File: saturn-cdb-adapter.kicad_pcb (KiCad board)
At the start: 2 copper layers, 76.2 x 76.2 mm, 60 parts, among them P1 CONN_02X22, P2 CONN_02X20, P3 CONN_02X20, P4 CONN_02X20, P5 CONN_02X20, U1 SH1, U2 MT28EW_FLASH

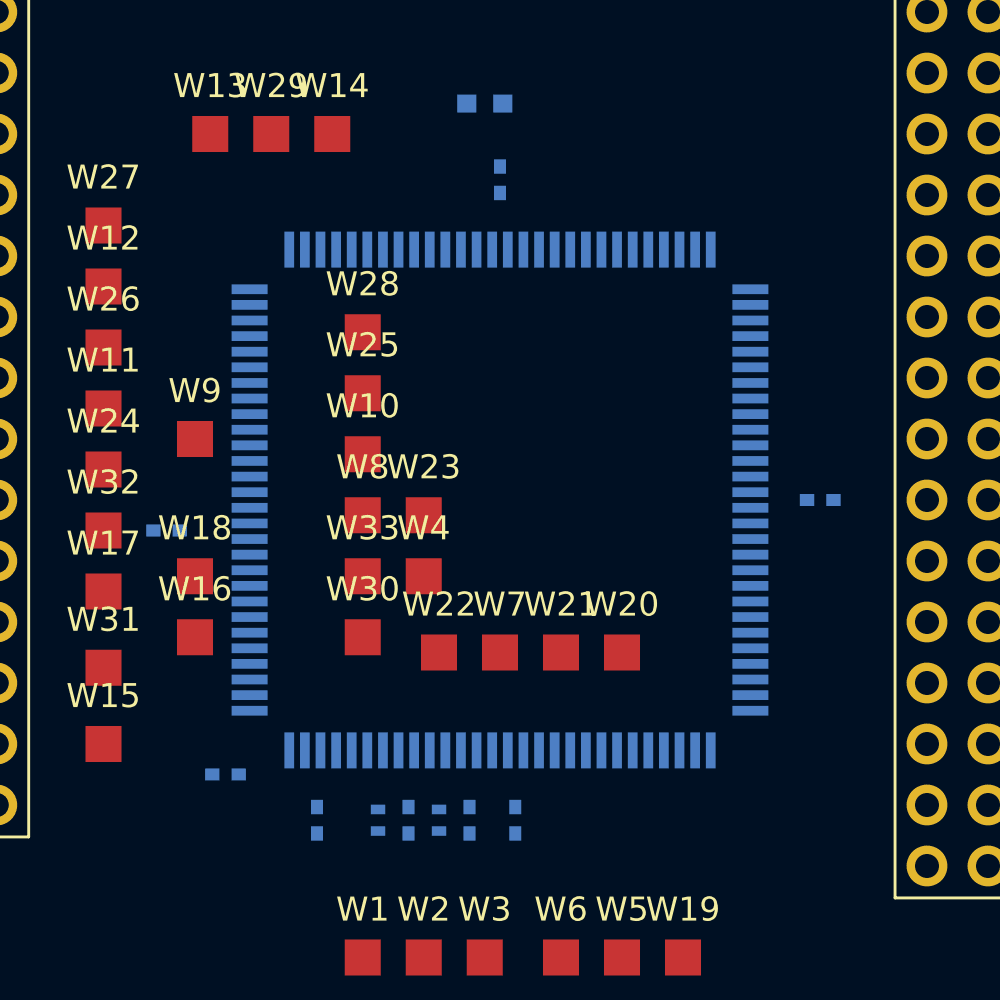
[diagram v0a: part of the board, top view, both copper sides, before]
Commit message: Fix sh1 footprint some more
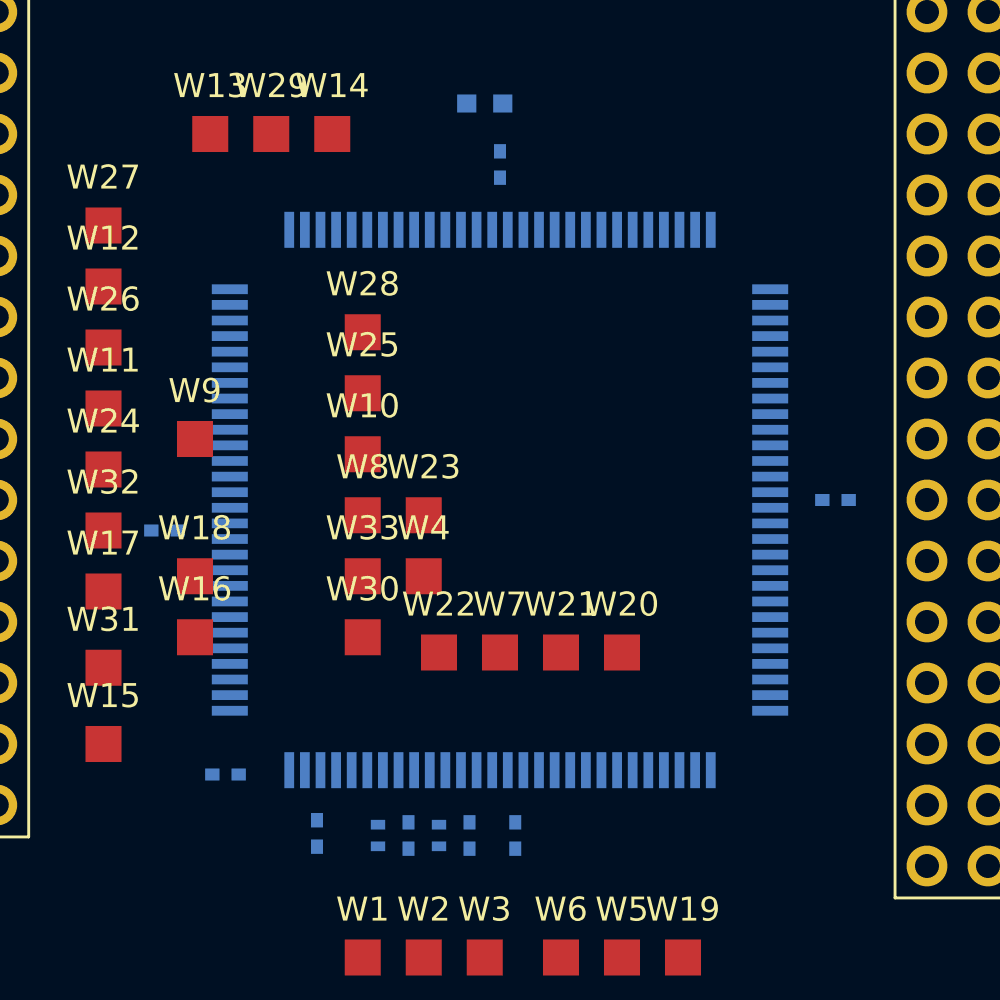
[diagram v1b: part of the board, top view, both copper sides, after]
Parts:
- moved C2 0.64 mm to (100.3, 99.1)
- moved C3 0.64 mm to (87.0, 113.0)
- moved C4 0.64 mm to (85.1, 113.0)
- moved C5 0.64 mm to (82.5, 113.0)
- moved R1 0.64 mm to (81.3, 113.0)
- moved R2 0.64 mm to (83.8, 113.0)
- moved C1 0.63 mm to (86.4, 85.1)
- moved C6 0.55 mm to (78.7, 112.9)
- moved C8 0.08 mm to (72.4, 100.3)

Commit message: More minor adjustments
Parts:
- moved W23 13.4 mm to (69.8, 99.1)
- moved W30 11.0 mm to (69.8, 106.7)
- moved W10 10.8 mm to (69.8, 96.5)
- moved W33 10.8 mm to (69.8, 101.6)
- moved W15 9.16 mm to (77.5, 104.1)
- moved W8 8.25 mm to (72.4, 99.7)
- moved W27 8.03 mm to (77.5, 90.2)
- moved W32 7.73 mm to (77.5, 101.6)
- moved C12 6.02 mm to (91.4, 84.5)
- moved W28 5.46 mm to (77.5, 87.6)
- moved W18 4.96 mm to (77.5, 99.1)
- moved W4 4.84 mm to (81.3, 106.7)
- moved W13 4.26 mm to (72.4, 87.6)
- moved W16 3.86 mm to (69.8, 104.1)
- moved W9 3.81 mm to (77.5, 96.5)
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
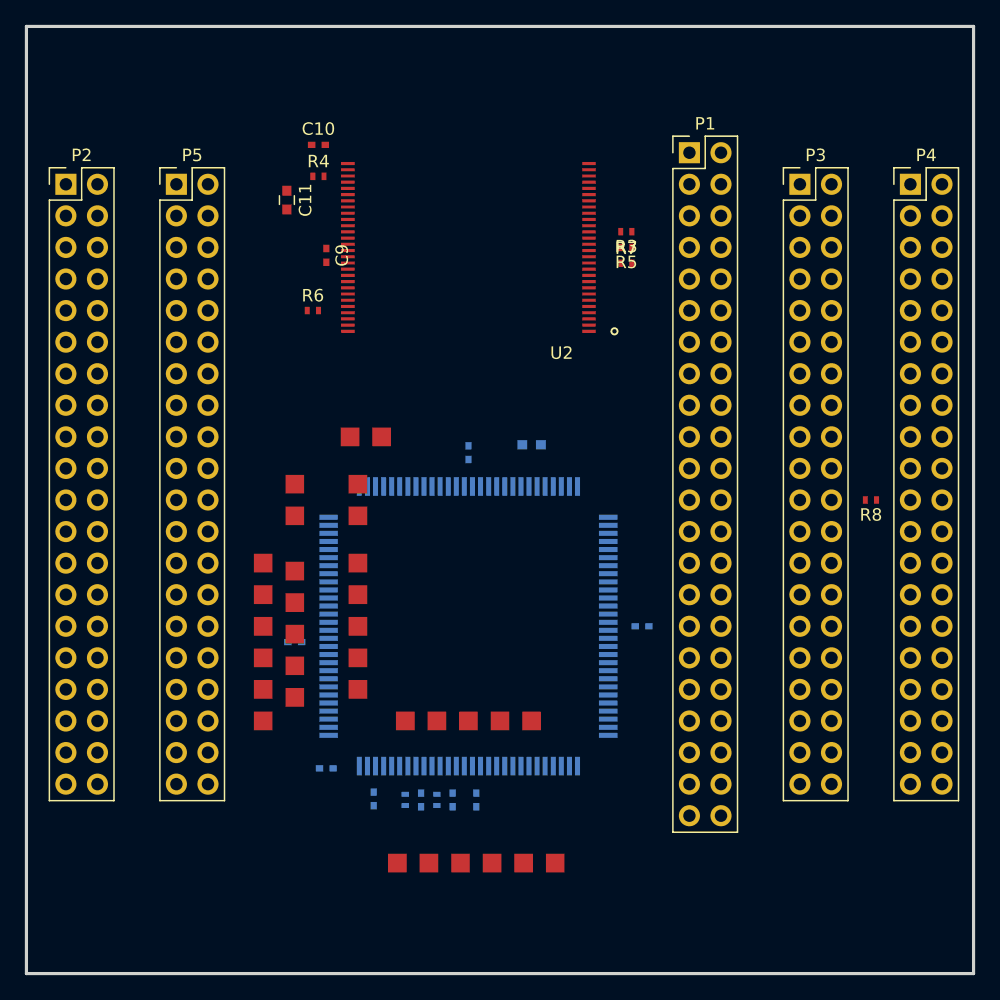
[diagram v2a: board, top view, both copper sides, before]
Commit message: Initial very rough route for most signals
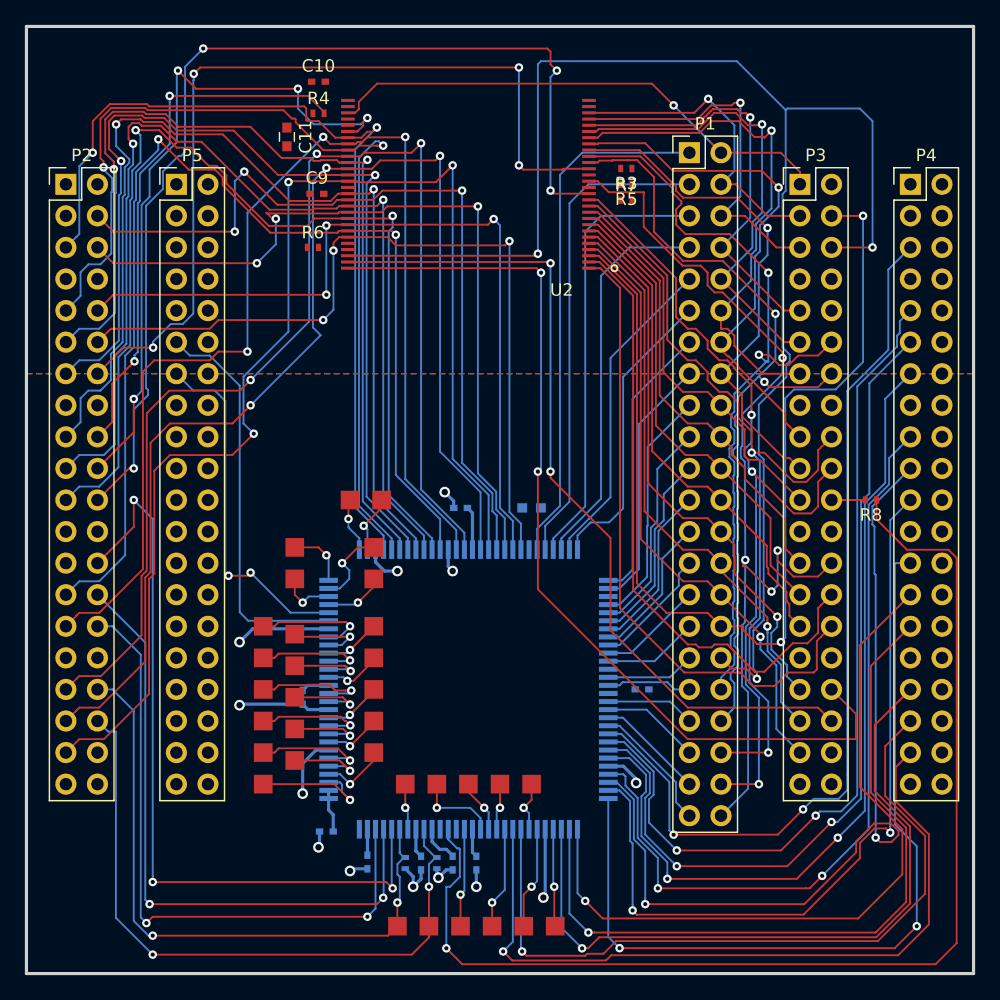
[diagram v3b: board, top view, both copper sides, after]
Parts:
- moved W32 5.24 mm to (78.7, 106.7)
- moved W15 5.24 mm to (78.7, 109.2)
- moved W18 5.24 mm to (78.7, 104.1)
- moved W25 5.24 mm to (78.7, 99.1)
- moved W27 5.24 mm to (78.7, 95.2)
- moved W28 5.24 mm to (78.7, 92.7)
- moved W9 5.24 mm to (78.7, 101.6)
- moved C6 5.11 mm to (78.2, 118.0)
- moved W14 5.08 mm to (79.4, 88.9)
- moved W29 5.08 mm to (76.8, 88.9)
- moved W33 5.08 mm to (69.8, 106.7)
- moved W8 5.08 mm to (72.4, 104.8)
- moved C10 5.08 mm to (74.3, 55.2)
- moved R3 5.08 mm to (99.1, 62.2)
- moved R4 5.08 mm to (74.3, 57.8)
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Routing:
- net FLASH_A16: track 0.00 -> 124.5 mm, vias 0 -> 3
- net AD11: track 0.00 -> 104.0 mm, vias 0 -> 3
- net AD10: track 0.00 -> 100.2 mm, vias 0 -> 3
- net AD9: track 0.00 -> 98.9 mm, vias 0 -> 3
- net AD8: track 0.00 -> 94.8 mm, vias 0 -> 3
- net CPU_CLK: track 0.00 -> 93.2 mm, vias 0 -> 1
- net AD7: track 0.00 -> 90.2 mm, vias 0 -> 2
- net AD6: track 0.00 -> 86.3 mm, vias 0 -> 2
- net AD5: track 0.00 -> 84.4 mm, vias 0 -> 2
- net FLASH_A15: track 0.00 -> 83.8 mm, vias 0 -> 2
- net ~FLASH_WE: track 0.00 -> 83.2 mm, vias 0 -> 4
- net AD4: track 0.00 -> 82.7 mm, vias 0 -> 2
- net AD3: track 0.00 -> 78.9 mm, vias 0 -> 2
- net AD1: track 0.00 -> 78.0 mm, vias 0 -> 2
- net FLASH_A21: track 0.00 -> 76.9 mm, vias 0 -> 4
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- added copper zone on B.Cu, net GND
- added copper zone on F.Cu, net GND

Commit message: Initial all signals connected
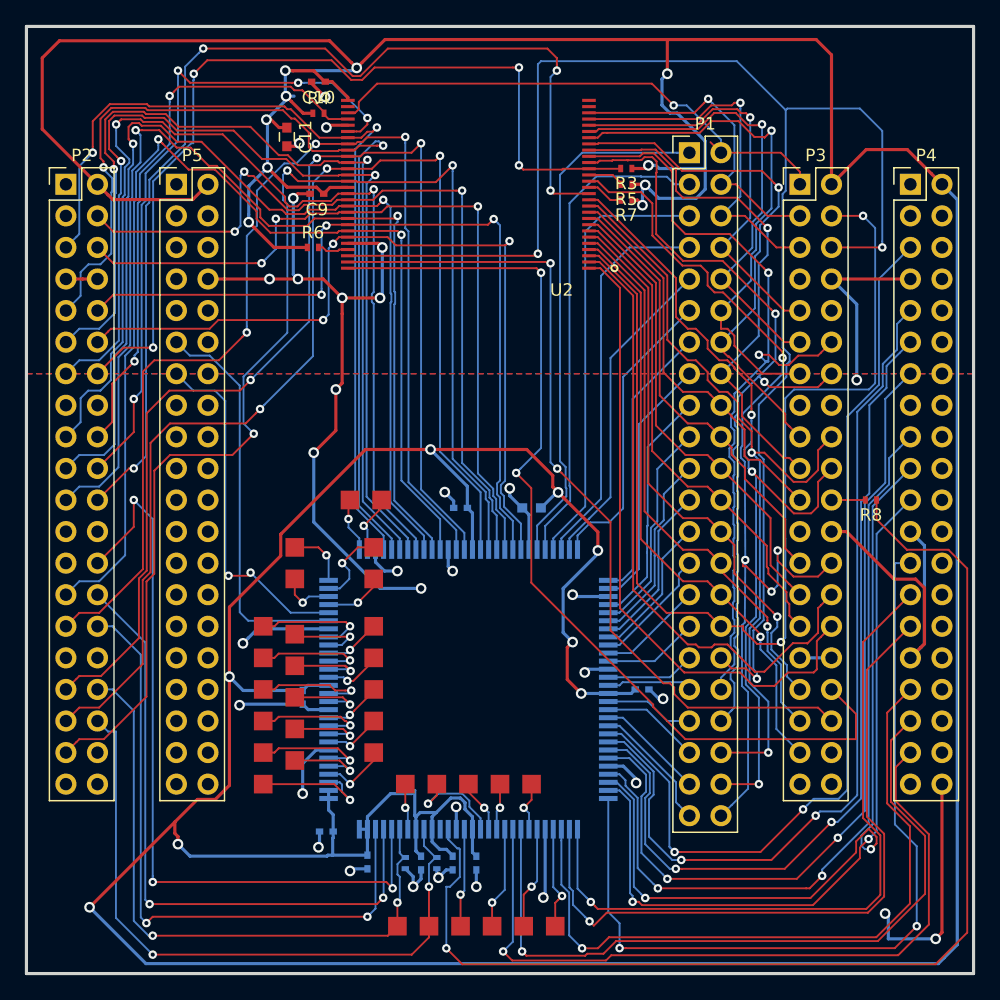
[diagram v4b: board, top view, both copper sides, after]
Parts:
- turned C10 to 180 degrees
- turned C2 to 0 degrees
- turned C9 to 180 degrees
- turned R7 to 180 degrees
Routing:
- net +3V3: track 19.1 -> 476.9 mm, vias 0 -> 18
- net GND: track 44.6 -> 188.0 mm, vias 13 -> 33
- net CPU_~WRH~/~LBS~: track 60.2 -> 56.7 mm
- net FLASH_READY: track 69.4 -> 72.8 mm
- net Net-(R7-Pad2): track 0.00 -> 2.97 mm
- net Net-(R5-Pad2): track 0.00 -> 2.92 mm
- net ~FLASH_CE: track 42.9 -> 45.7 mm
- net CPU_~WRL~/~WR: track 59.2 -> 56.6 mm
- net Net-(R6-Pad2): track 0.00 -> 2.53 mm
- net FLASH_A15: track 83.8 -> 86.2 mm
- net CPU_~CS6: track 63.0 -> 60.8 mm
- net CPU_~CS5: track 68.9 -> 66.7 mm
- net CPU_~CS0: track 72.1 -> 74.1 mm
- net Net-(U1-Pad69): track 6.66 -> 8.46 mm
- net AD11: track 104.0 -> 105.6 mm
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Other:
- net class Power: clearance 0.254 -> 0.1524

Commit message: SH power into star; minor cleanup
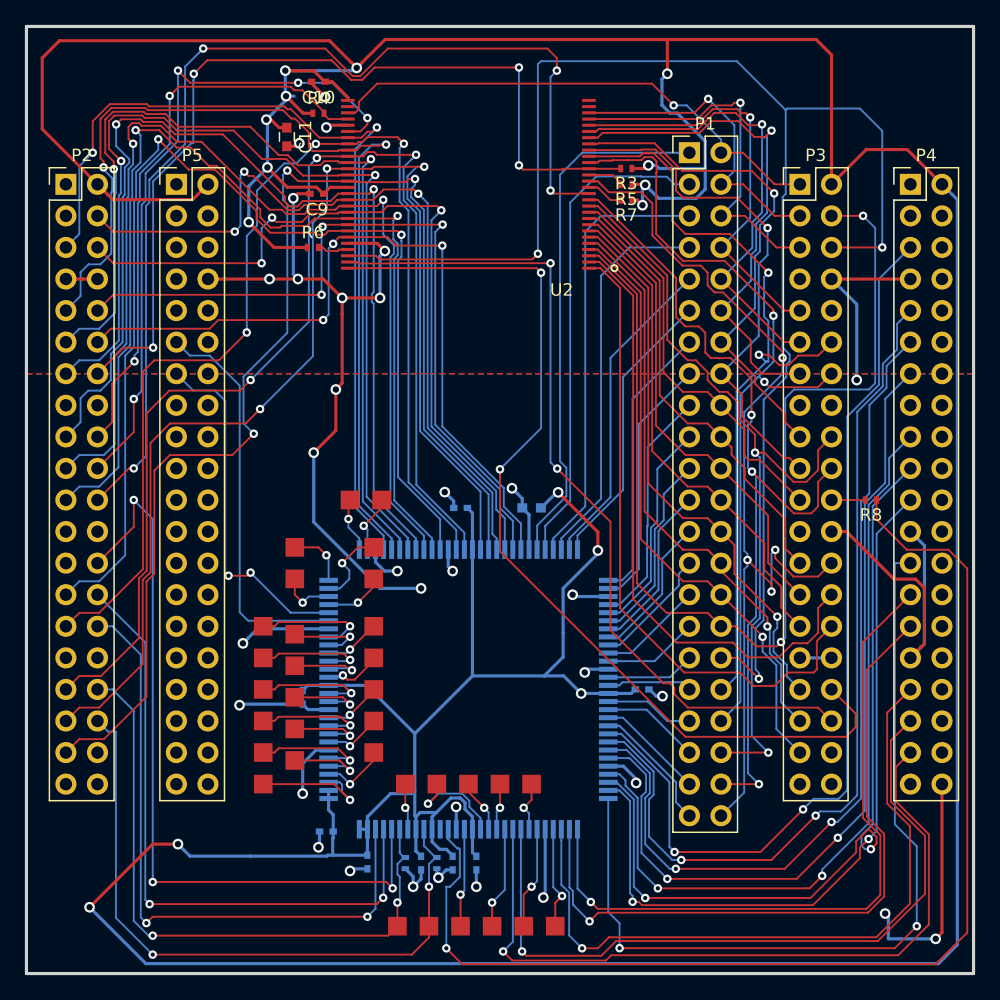
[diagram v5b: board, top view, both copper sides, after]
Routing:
- net +3V3: track 476.9 -> 445.0 mm, vias 18 -> 15
- net AD15: track 66.2 -> 61.8 mm
- net AD11: track 105.6 -> 102.6 mm
- net AD14: track 65.4 -> 62.8 mm
- net AD12: track 66.2 -> 64.1 mm
- net FLASH_A0: track 43.4 -> 41.7 mm
- net FLASH_A18: track 66.6 -> 65.2 mm
- net /Flash and CPU/CPU_A5: track 23.8 -> 23.0 mm
- net FLASH_A6: track 41.4 -> 40.6 mm
- net FLASH_A17: track 65.1 -> 64.3 mm
- net FLASH_A21: track 76.8 -> 76.0 mm
- net FLASH_A22: track 51.0 -> 50.2 mm
- net AD13: track 63.0 -> 62.2 mm
- net AD9: track 98.5 -> 97.9 mm

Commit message: Trace cleanup
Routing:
- net GND: track 187.8 -> 246.7 mm, vias 33 -> 62
- net +3V3: track 445.0 -> 417.1 mm, vias 15 -> 13
- net FLASH_A16: track 125.7 -> 106.8 mm, vias 3 -> 2
- net CPU_~CS7: track 68.2 -> 56.9 mm
- net FLASH_A24: track 78.4 -> 89.1 mm
- net MD0: track 62.0 -> 54.8 mm, vias 3 -> 2
- net CPU_~WRL~/~WR: track 56.6 -> 61.2 mm
- net /Flash and CPU/CPU_A2: track 35.6 -> 31.4 mm
- net CPU_~CS5: track 66.7 -> 63.1 mm
- net FLASH_A25: track 69.3 -> 72.8 mm
- net CPU_~WRH~/~LBS~: track 56.4 -> 59.9 mm
- net /Flash and CPU/CPU_A3: track 31.4 -> 28.6 mm
- net MD1: track 51.2 -> 53.4 mm
- net /Flash and CPU/CPU_A0: track 42.5 -> 44.7 mm
- net ~FLASH_WE: track 84.7 -> 82.8 mm
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
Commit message: Optimize more other than power
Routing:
- net GND: track 246.7 -> 301.1 mm, vias 62 -> 64
- net FLASH_A24: track 89.1 -> 77.5 mm
- net /Flash and CPU/CPU_A0: track 44.7 -> 37.6 mm
- net /Flash and CPU/CPU_A1: track 41.0 -> 34.2 mm
- net FLASH_A15: track 86.6 -> 82.5 mm
- net FLASH_A20: track 69.9 -> 66.5 mm
- net FLASH_A25: track 72.8 -> 69.7 mm
- net FLASH_A21: track 77.6 -> 80.8 mm
- net +3V3: track 417.1 -> 414.5 mm
- net FLASH_A16: track 106.8 -> 108.5 mm, vias 2 -> 3
- net AD10: track 100.8 -> 99.7 mm
- net AD12: track 65.2 -> 64.1 mm
- net FLASH_A17: track 63.9 -> 62.8 mm
- net AD11: track 103.7 -> 102.8 mm
- net FLASH_A1: track 25.6 -> 26.2 mm
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
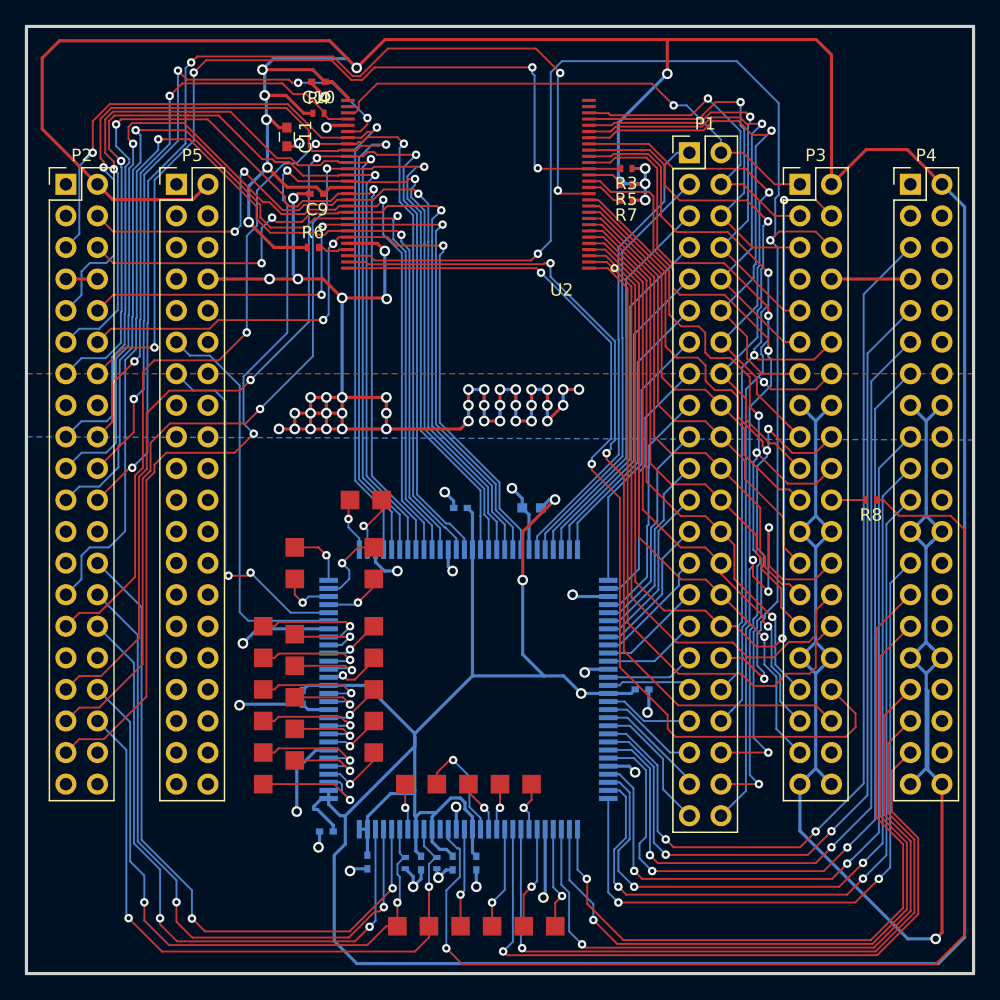
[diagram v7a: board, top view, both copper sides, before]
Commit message: Optimize power a bit
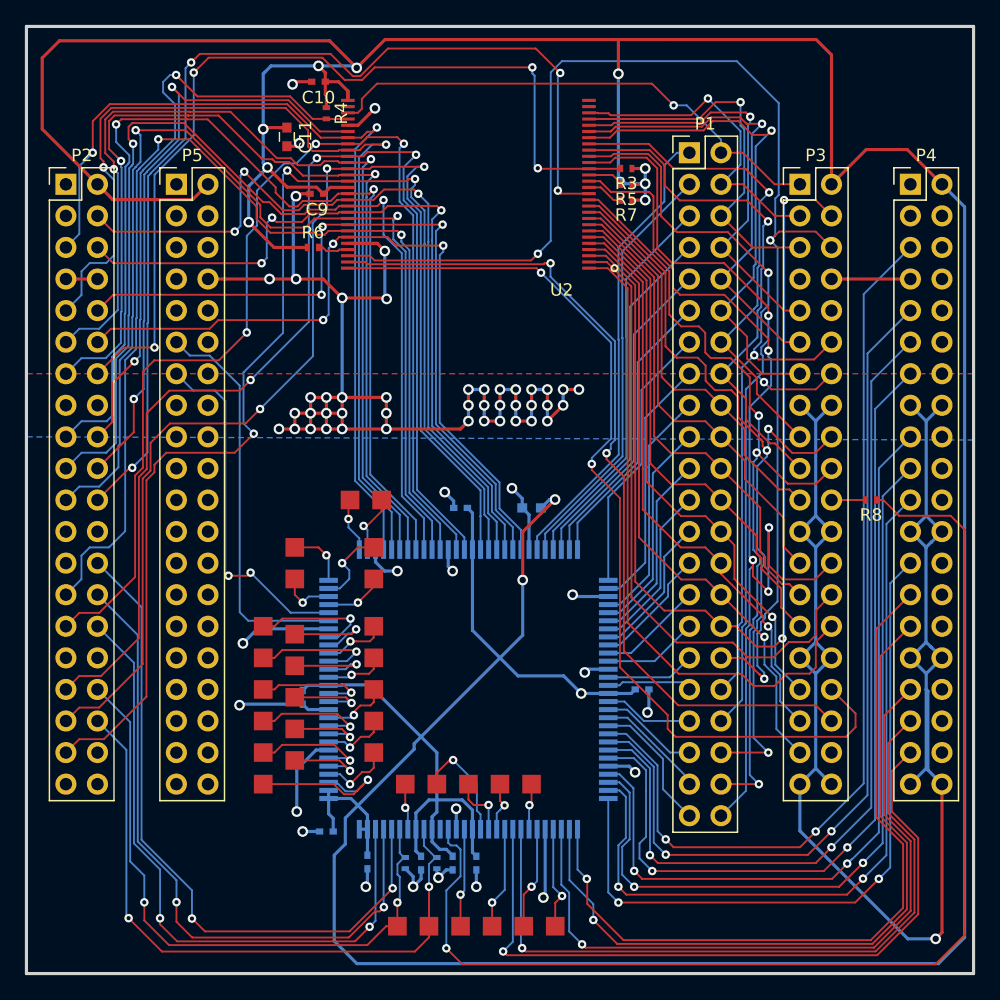
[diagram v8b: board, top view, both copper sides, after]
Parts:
- moved R4 0.64 mm to (74.9, 57.8), turned to 270 degrees
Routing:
- net +3V3: track 414.5 -> 402.6 mm, vias 13 -> 12
- net ~FLASH_OE: track 53.8 -> 49.3 mm, vias 4 -> 2
- net Net-(U1-Pad87): track 10.2 -> 13.1 mm
- net ~FLASH_CE: track 45.9 -> 48.1 mm
- net Net-(U1-Pad104): track 6.53 -> 7.83 mm
- net Net-(U1-Pad102): track 9.12 -> 10.4 mm
- net Net-(U1-Pad101): track 6.72 -> 7.44 mm
- net Net-(U1-Pad68): track 4.30 -> 5.00 mm
- net Net-(U1-Pad95): track 4.65 -> 5.33 mm
- net Net-(U1-Pad103): track 4.52 -> 5.10 mm
- net GND: track 301.1 -> 301.6 mm
- net Net-(U1-Pad105): track 9.37 -> 9.94 mm
- net Net-(U1-Pad92): track 4.68 -> 5.23 mm
